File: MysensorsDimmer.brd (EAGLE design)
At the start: 62 x 53 mm, 58 parts, among them IC1 7805DT, IC2 AT25DF512C-SSHN-B, IC3 ATSHA204A, J1 22-27-2021-02, J2 22-27-2021-02, J3 22-27-2021-02, J4 22-27-2021-02, J5 22-27-2021-02, M1 WIRELESS-NRF24L01, Q1 IRF530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

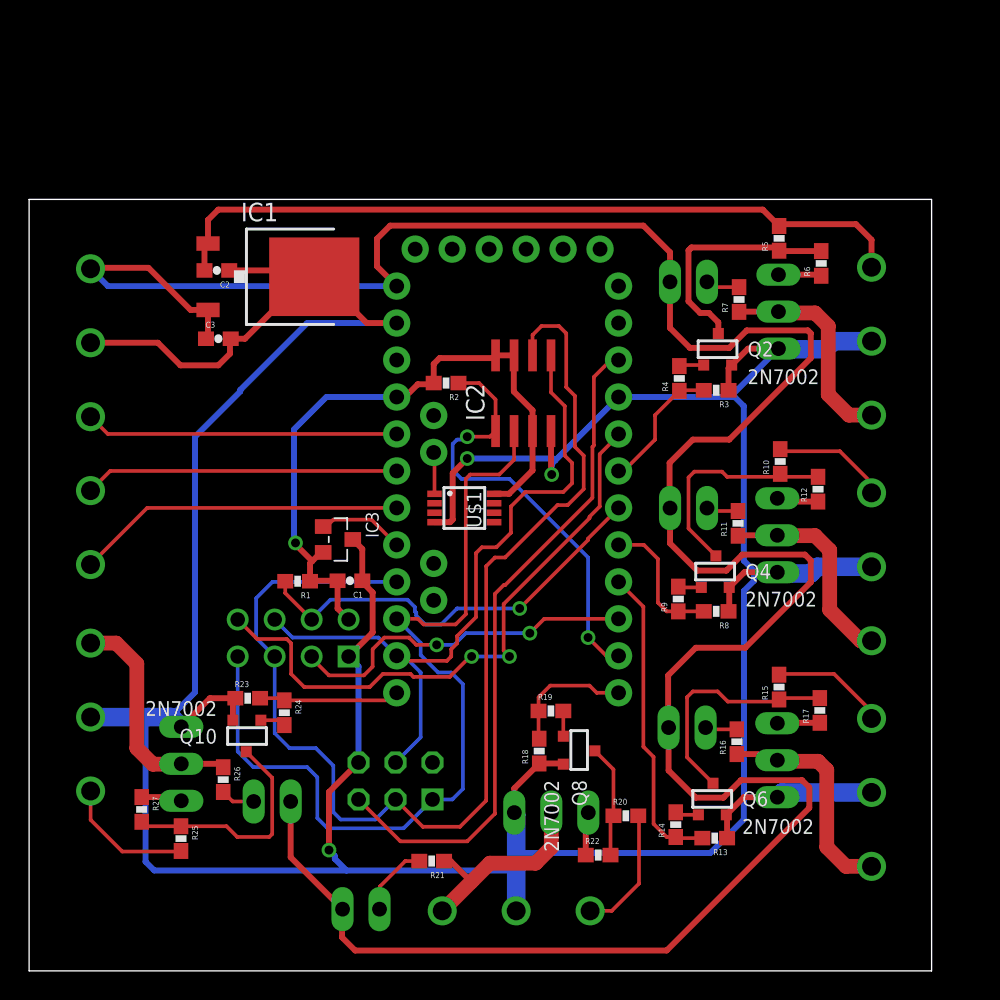
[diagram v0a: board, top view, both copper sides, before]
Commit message: corrected descriptions, names, etc.
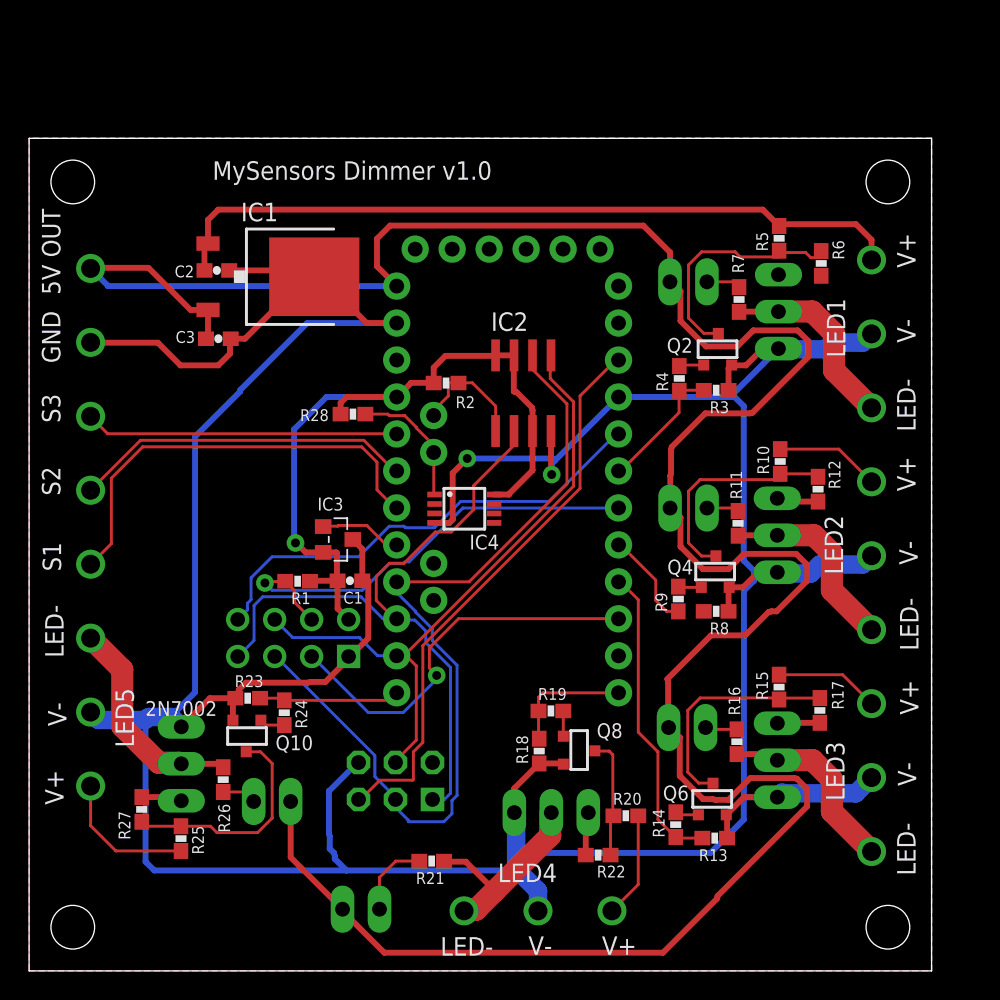
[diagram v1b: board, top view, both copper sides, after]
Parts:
- removed U$1: DS1820, Ava:µSOP8
- removed X4, X5: MKDSN1,5/3-5,08, con-phoenix-508:MKDSN1,5/3-5,08
- removed X6: MKDSN1,5/5-5,08, con-phoenix-508:MKDSN1,5/5-5,08
- added IC4: DS1820, Ava:µSOP8
- added R28: 4.7k, SparkFun-Passives:0603-RES
- X1: value MKDSN1,5/3-5,08 -> MKDSN1,5/9-5,08; device con-phoenix-508:MKDSN1,5/3-5,08 -> con-phoenix-508:MKDSN1,5/9-5,08
- X2: value MKDSN1,5/3-5,08 -> MKDSN1,5/8-5,08; device con-phoenix-508:MKDSN1,5/3-5,08 -> con-phoenix-508:MKDSN1,5/8-5,08
- moved X2 54.0 mm to (4.20, 30.5), turned to 90 degrees
- moved X3 26.1 mm to (32.4, 4.10), turned to 0 degrees
- moved X1 12.2 mm to (57.9, 28.5)
- renumbered JP2 to ISP, M1 to NRF24L01
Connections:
- removed net D8: ARDUINO1.8, IC2.1, R2.1
- new net A5: ARDUINO1.A5, IC2.1, R2.1
- net 5V: now also X2.8; no longer X6.5
- net A1: now also X2.4; no longer X6.1
- net A2: now also X2.5; no longer X6.2
- net A3: now also X2.6; no longer X6.3
- net A4: now also IC4.1, R28.1; no longer U$1.1
- net GND: now also IC4.4, X1.5, X1.8, X2.7; no longer U$1.4, X4.2, X5.2, X6.4
- net N$1: now also X1.6; no longer X2.3
- net N$10: now also X1.9; no longer X3.3
- net N$15: now also X3.3; no longer X4.3
- net N$20: now also X2.3; no longer X5.3
- net N$26: now also X1.4; no longer X2.1
- net N$27: now also X1.7; no longer X3.1
- net N$28: now also X3.1; no longer X4.1
- net N$29: now also X2.1; no longer X5.1
- net VCC: now also IC4.8, R28.2; no longer U$1.8
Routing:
- net D8: track 30.2 -> 0.00 mm, vias 2 -> 0
- net SCK: track 81.2 -> 60.5 mm
- net MISO: track 61.4 -> 49.0 mm
- net D2: track 41.6 -> 32.7 mm, vias 2 -> 0
- net A5: track 0.00 -> 8.30 mm
- net RST: track 46.4 -> 39.1 mm
- net A1: track 22.6 -> 29.9 mm
- net A4: track 2.86 -> 8.99 mm
- net VCC: track 46.4 -> 52.3 mm
- net MOSI: track 49.3 -> 44.5 mm
- net GND: track 280.2 -> 283.8 mm, vias 3 -> 2
- net 5V: track 185.3 -> 181.9 mm
- net N$2: track 2.97 -> 0.00 mm
- net D7: track 24.4 -> 27.4 mm, vias 2 -> 1
- net D5: track 9.51 -> 6.82 mm
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- added copper zone on layer 1, net GND
- added copper zone on layer 16, net GND
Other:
- board size 62 x 53 mm -> 62 x 57.2 mm
- board text added: "5V OUT"
- board text added: "GND"
- board text added: "LED-"
- board text added: "LED1"
- board text added: "LED2"
- board text added: "LED3"
- board text added: "LED4"
- board text added: "LED5"
- board text added: "MySensors Dimmer v1.0"
- board text added: "S1"
- board text added: "S2"
- board text added: "S3"
- board text added: "V+"
- board text added: "V-"

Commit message: adapted to SUPERTRONIC PP83N enclosure + corrected nrf module position in relation to screw connectors (they were overlaping)
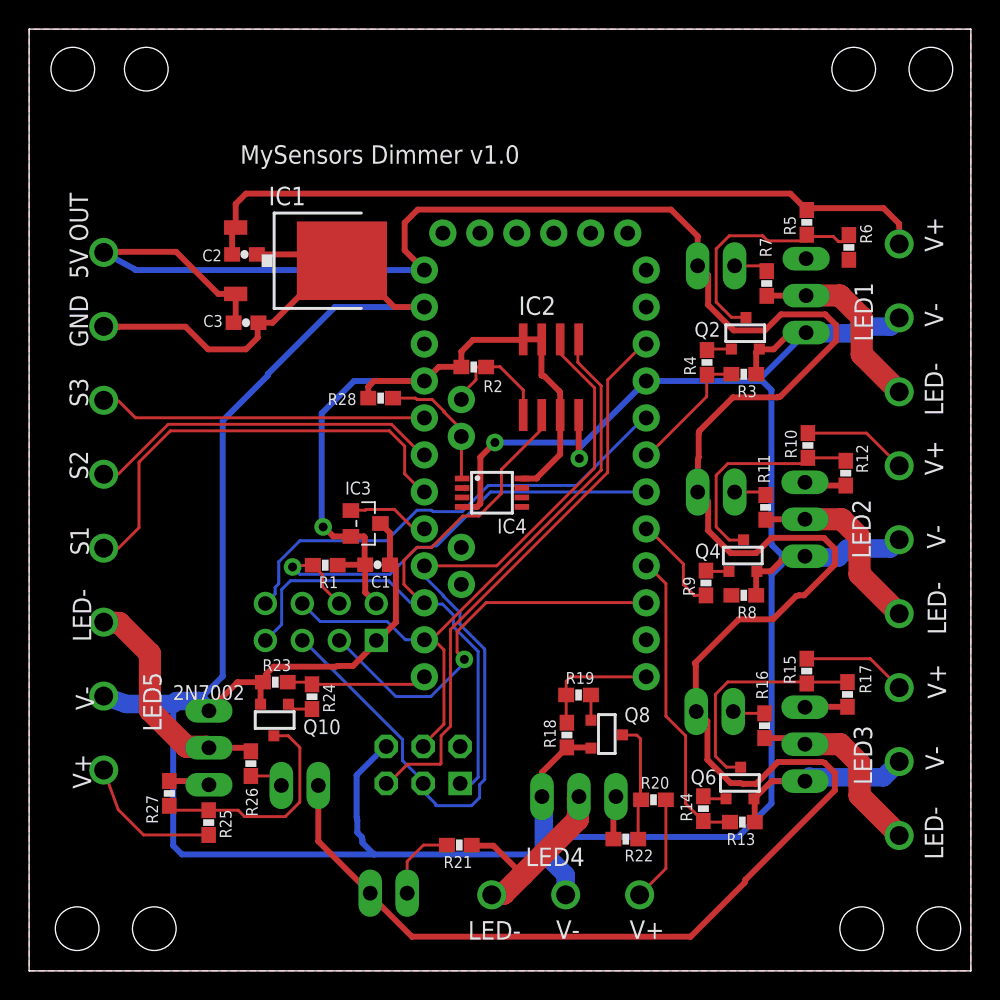
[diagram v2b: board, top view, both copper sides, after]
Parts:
- moved Q1 2.20 mm to (50.8, 46.4)
- moved R14 2.20 mm to (46.3, 11.1)
- moved R18 2.20 mm to (36.9, 16.2)
- moved C1 2.20 mm to (23.9, 27.9)
- moved IC4 2.20 mm to (31.8, 32.9)
- moved R21 2.20 mm to (29.6, 8.64)
- moved J4 2.20 mm to (24.7, 5.34)
- moved C2 2.20 mm to (14.8, 49.2)
- moved IC3 2.20 mm to (23.1, 30.7)
- moved NRF24L01 2.20 mm to (17.5, 35.4)
- moved R24 2.20 mm to (19.4, 18.8)
- moved R25 2.20 mm to (12.3, 10.2)
- moved Q9 2.20 mm to (14.9, 15.3)
- moved R26 2.20 mm to (15.2, 14.2)
- moved R27 2.20 mm to (9.63, 12.2)
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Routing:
- net GND: track 283.8 -> 285.6 mm
- net 5V: track 181.9 -> 183.7 mm
- net A1: track 29.9 -> 30.9 mm
- net A2: track 23.3 -> 24.3 mm
- net N$20: track 15.0 -> 16.0 mm
- net A3: track 21.5 -> 22.5 mm
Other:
- board size 62 x 57.2 mm -> 64.7 x 64.7 mm
